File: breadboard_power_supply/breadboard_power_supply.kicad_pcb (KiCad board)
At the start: 2 copper layers, 34.2 x 58.5 mm, 17 parts, among them J1 Conn_01x02_Pin, J2 Conn_01x02_Pin, J3 Conn_01x03_Pin, J4 Conn_01x03_Pin, J5 Screw_Terminal_01x02, J6 Barrel_Jack_PTH, J7 Screw_Terminal_01x02, U2 LM317_TO-220, U3 LM7805_TO220

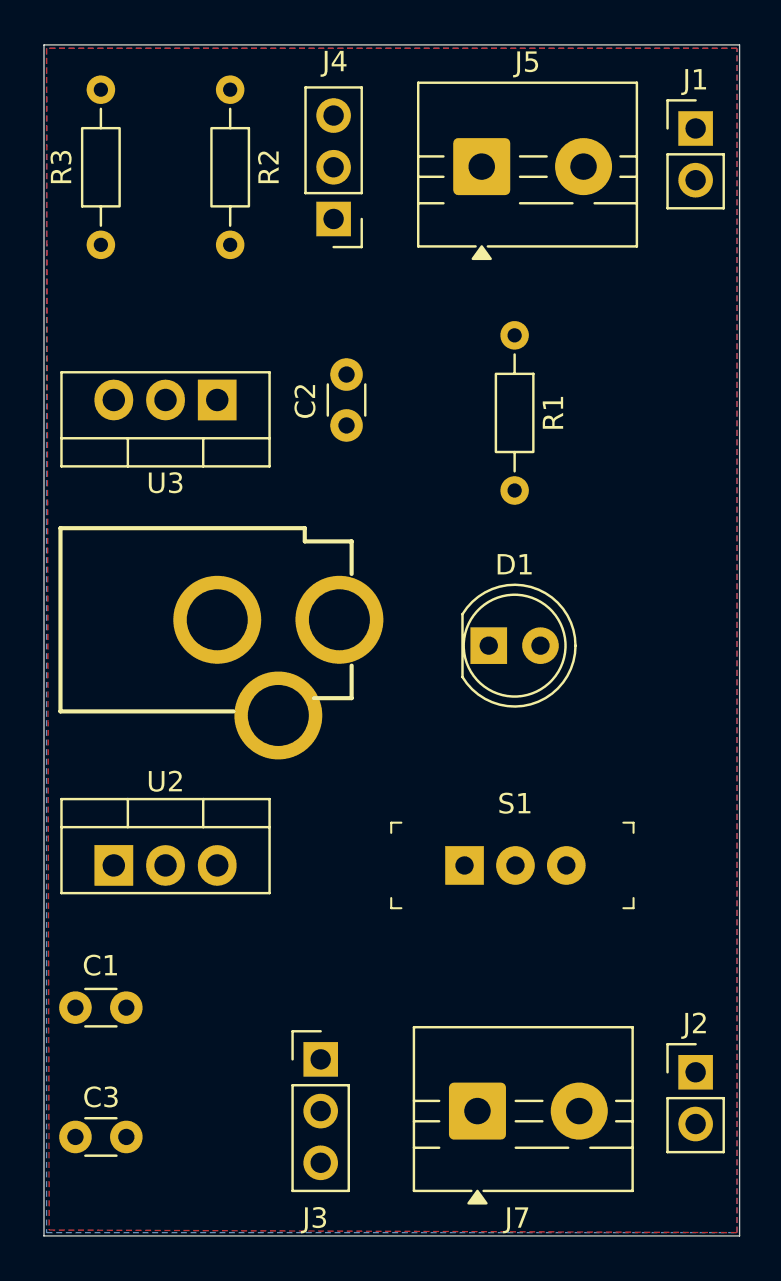
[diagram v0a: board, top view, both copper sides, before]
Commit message: front and back copper pour
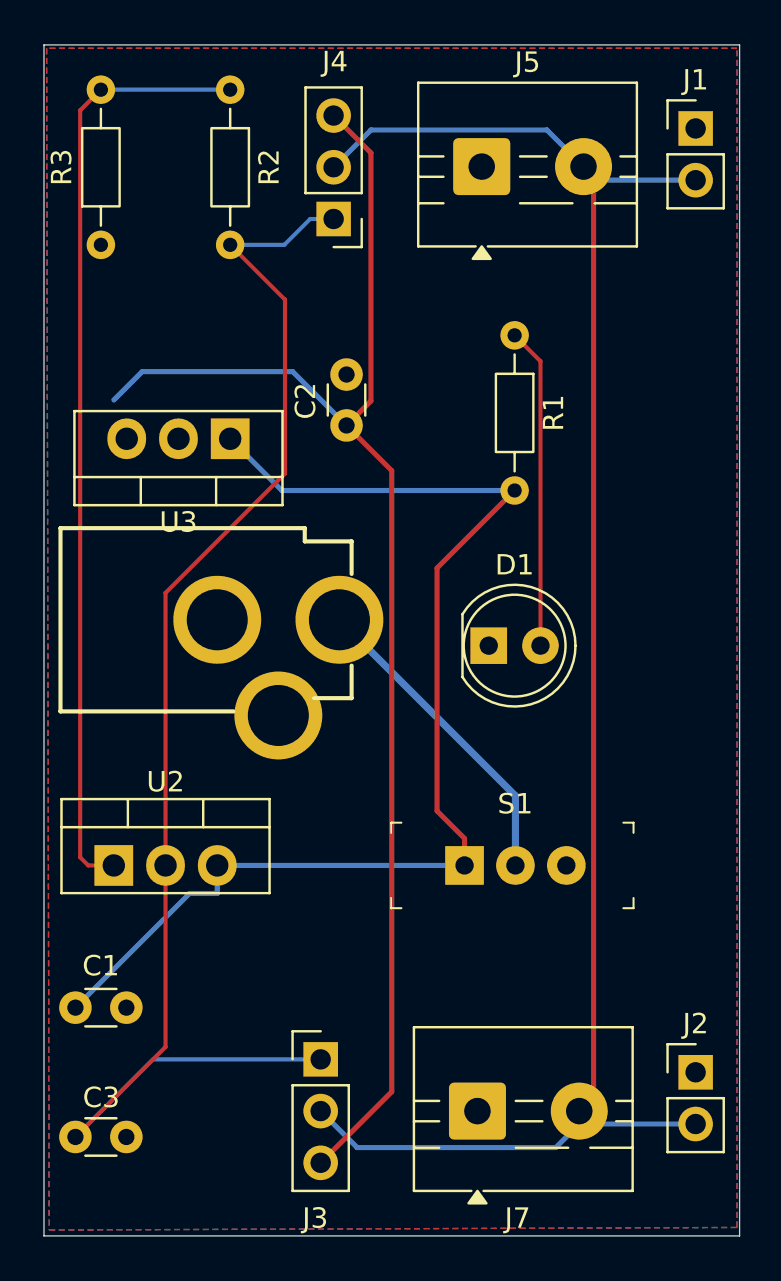
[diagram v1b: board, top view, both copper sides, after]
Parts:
- moved U3 2.01 mm to (184.8, 95.2)
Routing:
- net /PWR_OUTPUT: track 0.00 -> 86.7 mm
- net /3.3V: track 0.00 -> 68.4 mm
- net /5V: track 0.00 -> 68.2 mm
- net /12V: track 0.00 -> 58.4 mm
- net Net-(U2-ADJ): track 0.00 -> 46.3 mm
- net Net-(D1-Pad2): track 0.00 -> 15.8 mm
- net /PWR_INPUT: track 0.00 -> 15.6 mm
